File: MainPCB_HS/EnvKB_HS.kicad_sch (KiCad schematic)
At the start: 205 parts

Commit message: Added ANSI layout keys back.
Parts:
- added Stab5, Stab6: Stabilizer, Mounting_Keyboard_Stabilizer:Stabilizer_Cherry_MX_2u, symbol Mechanical:MountingHole
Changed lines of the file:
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@@
     (pin "2")
+  )
+  (symbol (lib_id "Mechanical:MountingHole") (at 172.72 259.842 0) (mirror x) (unit 1)
+    (in_bom yes) (on_board yes)
+    (property "Reference" "Stab5" (id 0) (at 170.2054 258.6736 0)
+      (effects (font (size 1.27 1.27)) (justify right))
+    )
+    (property "Value" "Stabilizer" (id 1) (at 170.2054 260.985 0)
+      (effects (font (size 1.27 1.27)) (justify right))
+    )
+    (property "Footprint" "Mounting_Keyboard_Stabilizer:Stabilizer_Cherry_MX_2u" (id 2) (at 172.72 259.842 0)
+      (effects (font (size 1.27 1.27)) hide)
+    )
+    (property "Datasheet" "~" (id 3) (at 172.72 259.842 0)
+      (effects (font (size 1.27 1.27)) hide)
+    )
   )
   (symbol (lib_id "Device:R_Small") (at 227.965 198.12 0) (unit 1)
@@
     (pin "1")
     (pin "2")
+  )
+  (symbol (lib_id "Mechanical:MountingHole") (at 187.198 259.842 0) (mirror x) (unit 1)
+    (in_bom yes) (on_board yes)
+    (property "Reference" "Stab6" (id 0) (at 184.6834 258.6736 0)
+      (effects (font (size 1.27 1.27)) (justify right))
+    )
+    (property "Value" "Stabilizer" (id 1) (at 184.6834 260.985 0)
+      (effects (font (size 1.27 1.27)) (justify right))
+    )
+    (property "Footprint" "Mounting_Keyboard_Stabilizer:Stabilizer_Cherry_MX_2u" (id 2) (at 187.198 259.842 0)
+      (effects (font (size 1.27 1.27)) hide)
+    )
+    (property "Datasheet" "~" (id 3) (at 187.198 259.842 0)
+      (effects (font (size 1.27 1.27)) hide)
+    )
   )
   (symbol (lib_id "Device:R_Small") (at 221.615 198.12 180) (unit 1)
@@
       (reference "Stab4") (unit 1) (value "Stabilizer") (footprint "Mounting_Keyboard_Stabilizer:Stabilizer_Cherry_MX_2u")
     )
+    (path "/49fb1b93-ef2c-4c13-8861-864d83ebc2ed"
+      (reference "Stab5") (unit 1) (value "Stabilizer") (footprint "Mounting_Keyboard_Stabilizer:Stabilizer_Cherry_MX_2u")
+    )
+    (path "/b0e410f9-6c63-4cdc-9525-c65e9116bb6a"
+      (reference "Stab6") (unit 1) (value "Stabilizer") (footprint "Mounting_Keyboard_Stabilizer:Stabilizer_Cherry_MX_2u")
+    )
     (path "/00000000-0000-0000-0000-000060ac4d40"

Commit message: fixed? ansi+iso+hotswap support I think but also file cleanup
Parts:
- D0, D1, D10, D11, D12, D13, D14, D15, D16, D17, D18, D19, D2, D20, D21, D22, D23, D24, D25, D26, D27, D28, D29, D3, D30, D31, D32, D33, D34, D35, D36, D37, D38, D39, D4, D40, D41, D42, D43, D44, D45, D46, D47, D48, D49, D5, D50, D51, D52, D53, D54, D55, D56, D57, D58, D59, D6, D60, D61, D62, D63, D64, D65, D66, D67, D68, D69, D7, D70, D71, D72, D73, D74, D75, D76, D77, D78, D79, D8, D80, D81, D82, D83, D84, D85, D86, D87, D88, D9: value D -> (none); footprint EM_Extras:SOD-123+D_DO-35_SOD27_P7.62mm_Horizontal -> (none)
- H0, H1, H10, H2, H3, H4, H5, H6, H7, H9: value MountingHole -> (none); footprint MountingHole:MountingHole_2.2mm_M2_Pad -> (none)
- K_0, K_1, K_10, K_11, K_12, K_13, K_14, K_15, K_16, K_17, K_18, K_19, K_2, K_20, K_21, K_22, K_23, K_24, K_25, K_26, K_27, K_28, K_29, K_3, K_30, K_31, K_32, K_33, K_34, K_35, K_36, K_37, K_38, K_39, K_4, K_40, K_41, K_42, K_43, K_44, K_45, K_46, K_47, K_48, K_49, K_5, K_50, K_51, K_52, K_53, K_54, K_55, K_56, K_57, K_58, K_59, K_6, K_60, K_61, K_62, K_64, K_64B1, K_65, K_66, K_67, K_68, K_69, K_7, K_70, K_71, K_72, K_73, K_74, K_75, K_76, K_77, K_78, K_79, K_8, K_80, K_81, K_82, K_83, K_84, K_85, K_86, K_87, K_88, K_9: value KEYSW -> (none); footprint MX_Only:MXOnly-1U-Hotswap-Modified -> (none); LCSC (none) -> C2803348
- K_63, K_63B1: value MX-NoLED -> (none); footprint MX_Only:MXOnly-1U-Hotswap-Modified -> (none); LCSC (none) -> C2803348
- LEDRESISTOR1: value 5.1K Resistor 1/4w -> (none); footprint Resistor_THT:R_Axial_DIN0207_L6.3mm_D2.5mm_P10.16mm_Horizontal -> (none)
- LEDRESISTOR2: value 5.1K Resistor 0805 -> (none); footprint Resistor_SMD:R_0805_2012Metric_Pad1.20x1.40mm_HandSolder -> (none)
- PowerLED0: value LED 3MM -> (none); footprint LED_THT:LED_D3.0mm_FlatTop -> (none)
- PowerLED1: value LED 0805 -> (none); footprint LED_SMD:LED_0805_2012Metric -> (none)
- RESISTOR0: value 5.1kohm 1/4w -> (none); footprint Resistor_THT:R_Axial_DIN0207_L6.3mm_D2.5mm_P10.16mm_Horizontal -> (none)
- RESISTOR1: value 5.1kohm 1/4 -> (none); footprint Resistor_THT:R_Axial_DIN0207_L6.3mm_D2.5mm_P10.16mm_Horizontal -> (none)
- RESISTOR2, RESISTOR3: value 5.1kohm 0805 -> (none); footprint Resistor_SMD:R_0805_2012Metric -> (none)
- RPI0: value Pico -> (none); footprint EM_Extras:RPi_Pico_SMD_TH -> (none)
- SW-RST0: value EVQ -> (none); footprint Button_Switch_SMD:Panasonic_EVQPUM_EVQPUD -> (none)
- Stab1: value Stabilizer -> (none); footprint Mounting_Keyboard_Stabilizer:Stabilizer_Cherry_MX_6.25u -> (none)
- Stab2, Stab3, Stab4, Stab5, Stab6: value Stabilizer -> (none); footprint Mounting_Keyboard_Stabilizer:Stabilizer_Cherry_MX_2u -> (none)
- USB1: value TYPE-C-31-M-14 -> (none); footprint josh-connectors:USB_C_TYPE-C-31-M-14 -> (none)

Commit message: roundified hotswap board and general corrections to other boards, RP2040 DRC fixes mainly
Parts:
- added D89: 1n4002, Diode_THT:D_DO-41_SOD81_P7.62mm_Horizontal, symbol Device:D_Small
- D0, D1, D10, D11, D12, D13, D14, D15, D16, D17, D18, D19, D2, D20, D21, D22, D23, D24, D25, D26, D27, D28, D29, D3, D30, D31, D32, D33, D34, D35, D36, D37, D38, D39, D4, D40, D41, D42, D43, D44, D45, D46, D47, D48, D49, D5, D50, D51, D52, D53, D54, D55, D56, D57, D58, D59, D6, D60, D61, D62, D63, D64, D65, D66, D67, D68, D69, D7, D70, D71, D72, D73, D74, D75, D76, D77, D78, D79, D8, D80, D81, D82, D83, D84, D85, D86, D87, D88, D9: value (none) -> D; footprint (none) -> EM_Extras:SOD-123+D_DO-35_SOD27_P7.62mm_Horizontal
- H0, H1, H10, H2, H3, H4, H5, H6, H7, H9: value (none) -> MountingHole; footprint (none) -> MountingHole:MountingHole_2.2mm_M2_Pad
- K_0, K_1, K_10, K_11, K_12, K_13, K_14, K_15, K_16, K_17, K_18, K_19, K_2, K_20, K_21, K_22, K_23, K_24, K_25, K_26, K_27, K_28, K_29, K_3, K_30, K_31, K_32, K_33, K_34, K_35, K_36, K_37, K_38, K_39, K_4, K_40, K_41, K_42, K_43, K_44, K_45, K_46, K_47, K_48, K_49, K_5, K_50, K_51, K_52, K_53, K_54, K_55, K_56, K_57, K_58, K_59, K_6, K_60, K_61, K_62, K_64, K_64B1, K_65, K_66, K_67, K_68, K_69, K_7, K_70, K_71, K_72, K_73, K_74, K_75, K_76, K_77, K_78, K_79, K_8, K_80, K_81, K_82, K_83, K_84, K_85, K_86, K_87, K_88, K_9: value (none) -> KEYSW; footprint (none) -> MX_Only:MXOnly-1U-Hotswap-Modified
- K_63, K_63B1: value (none) -> MX-NoLED; footprint (none) -> MX_Only:MXOnly-1U-Hotswap-Modified
- LEDRESISTOR1: value (none) -> 5.1K Resistor 1/4w; footprint (none) -> Resistor_THT:R_Axial_DIN0207_L6.3mm_D2.5mm_P10.16mm_Horizontal
- LEDRESISTOR2: value (none) -> 5.1K Resistor 0805; footprint (none) -> Resistor_SMD:R_0805_2012Metric_Pad1.20x1.40mm_HandSolder
- PowerLED0: value (none) -> LED 3MM; footprint (none) -> LED_THT:LED_D3.0mm_FlatTop
- PowerLED1: value (none) -> LED 0805; footprint (none) -> LED_SMD:LED_0805_2012Metric
- RESISTOR0: value (none) -> 5.1kohm 1/4w; footprint (none) -> Resistor_THT:R_Axial_DIN0207_L6.3mm_D2.5mm_P10.16mm_Horizontal
- RESISTOR1: value (none) -> 5.1kohm 1/4; footprint (none) -> Resistor_THT:R_Axial_DIN0207_L6.3mm_D2.5mm_P10.16mm_Horizontal
- RESISTOR2, RESISTOR3: value (none) -> 5.1kohm 0805; footprint (none) -> Resistor_SMD:R_0805_2012Metric
- RPI0: value (none) -> Pico; footprint (none) -> EM_Extras:RPi_Pico_SMD_TH
- SW-RST0: value (none) -> EVQ; footprint (none) -> Button_Switch_SMD:Panasonic_EVQPUM_EVQPUD
- Stab1: value (none) -> Stabilizer; footprint (none) -> Mounting_Keyboard_Stabilizer:Stabilizer_Cherry_MX_6.25u
- Stab2, Stab3, Stab4, Stab5, Stab6: value (none) -> Stabilizer; footprint (none) -> Mounting_Keyboard_Stabilizer:Stabilizer_Cherry_MX_2u
- USB1: value (none) -> TYPE-C-31-M-14; footprint (none) -> josh-connectors:USB_C_TYPE-C-31-M-14
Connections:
- net USBVBUS: now also D89.2 (A); no longer RPI0.40 (VBUS)
- net VSYS: now reaches RPI0.39 (VSYS)
- net VSYS: now also D89.1 (K)

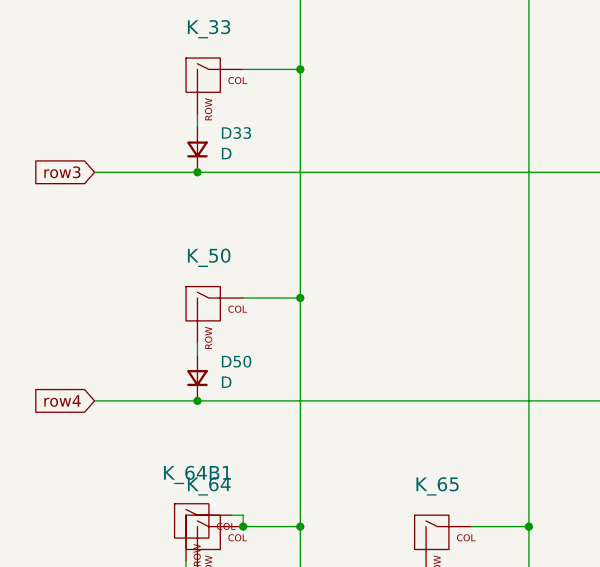
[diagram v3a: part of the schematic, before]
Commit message: Added Stepped left shift for orig version
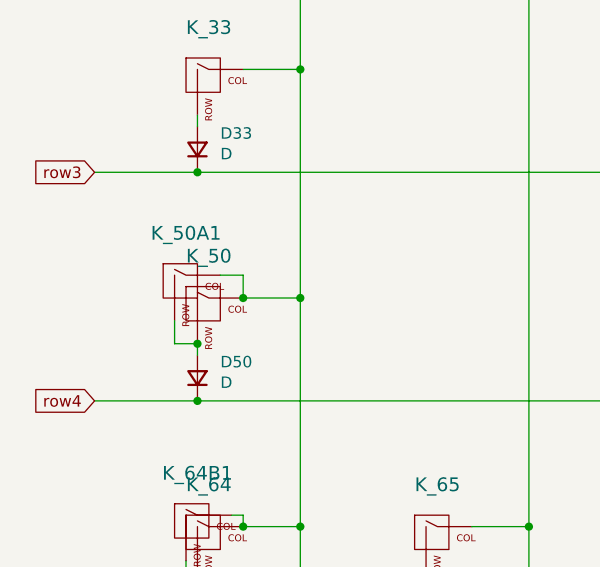
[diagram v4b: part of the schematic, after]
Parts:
- added K_50A1: KEYSW, MX_Only:MXOnly-1U-Hotswap-Modified, symbol MX_Alps_Hybrid:MX-NoLED
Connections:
- net col0: now also K_50A1.1 (COL)
- net at D50.2 (A), K_50.2 (ROW): now also K_50A1.2 (ROW)
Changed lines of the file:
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@@
   (junction (at 161.29 162.56) (diameter 0) (color 0 0 0 0)
   )
+  (junction (at 39.37 125.73) (diameter 0) (color 0 0 0 0)
+  )
   (junction (at 172.72 125.73) (diameter 0) (color 0 0 0 0)
   )
@@
   (junction (at 274.32 74.93) (diameter 0) (color 0 0 0 0)
   )
+  (junction (at 34.29 130.81) (diameter 0) (color 0 0 0 0)
+  )
   (junction (at 415.29 35.56) (diameter 0) (color 0 0 0 0)
   )
@@
     (stroke (width 0) (type default) (color 0 0 0 0))
   )
+  (wire (pts (xy 31.75 130.81) (xy 34.29 130.81))
+    (stroke (width 0) (type default) (color 0 0 0 0))
+  )
   (wire (pts (xy 110.49 137.16) (xy 135.89 137.16))
     (stroke (width 0) (type default) (color 0 0 0 0))
@@
     (stroke (width 0) (type default) (color 0 0 0 0))
   )
+  (wire (pts (xy 36.83 123.19) (xy 39.37 123.19))
+    (stroke (width 0) (type default) (color 0 0 0 0))
+  )
+  (wire (pts (xy 39.37 123.19) (xy 39.37 125.73))
+    (stroke (width 0) (type default) (color 0 0 0 0))
+  )
   (wire (pts (xy 221.615 200.66) (xy 221.615 201.295))
     (stroke (width 0) (type default) (color 0 0 0 0))
@@
     (stroke (width 0) (type default) (color 0 0 0 0))
   )
+  (wire (pts (xy 31.75 128.27) (xy 31.75 130.81))
+    (stroke (width 0) (type default) (color 0 0 0 0))
+  )
   (wire (pts (xy 191.77 125.73) (xy 198.12 125.73))
     (stroke (width 0) (type default) (color 0 0 0 0))
@@
     (pin "2")
   )
+  (symbol (lib_id "MX_Alps_Hybrid:MX-NoLED") (at 33.02 124.46 0) (unit 1)
+    (in_bom yes) (on_board yes)
+    (property "Reference" "K_50A1" (id 0) (at 33.02 118.5418 0)
+      (effects (font (size 1.524 1.524)))
+    )
+    (property "Value" "KEYSW" (id 1) (at 33.02 127 0)
+      (effects (font (size 1.524 1.524)) hide)
+    )
+    (property "Footprint" "MX_Only:MXOnly-1U-Hotswap-Modified" (id 2) (at 33.02 124.46 0)
+      (effects (font (size 1.524 1.524)) hide)
+    )
+    (property "Datasheet" "" (id 3) (at 33.02 124.46 0)
+      (effects (font (size 1.524 1.524)))
+    )
+    (property "LCSC" "C2803348" (id 4) (at 33.02 124.46 0)
+      (effects (font (size 1.27 1.27)) hide)
+    )
+    (pin "1")
+    (pin "2")
+  )
   (symbol (lib_id "Mechanical:MountingHole") (at 172.72 259.842 0) (mirror x) (unit 1)
     (in_bom yes) (on_board yes)
@@
       (reference "K_50") (unit 1) (value "KEYSW") (footprint "MX_Only:MXOnly-1U-Hotswap-Modified")
     )
+    (path "/413bf164-96e1-4397-9fa3-f110780c247f"
+      (reference "K_50A1") (unit 1) (value "KEYSW") (footprint "MX_Only:MXOnly-1U-Hotswap-Modified")
+    )
     (path "/00000000-0000-0000-0000-000000000511"

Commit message: enlarged mount holes on HS version + increased clearance on some traces between diodes and plates holes, need to do this for whole board though
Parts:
- H0, H1, H10, H2, H3, H4, H5, H6, H7, H9: footprint MountingHole:MountingHole_2.2mm_M2_Pad -> MountingHole:MountingHole_3.7mm_Pad
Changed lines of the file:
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@@
       (effects (font (size 1.27 1.27)) (justify left))
     )
-    (property "Footprint" "MountingHole:MountingHole_2.2mm_M2_Pad" (id 2) (at 147.32 270.51 0)
+    (property "Footprint" "MountingHole:MountingHole_3.7mm_Pad" (id 2) (at 147.32 270.51 0)
       (effects (font (size 1.27 1.27)) hide)
     )
@@
       (effects (font (size 1.27 1.27)) (justify left))
     )
-    (property "Footprint" "MountingHole:MountingHole_2.2mm_M2_Pad" (id 2) (at 137.16 270.51 0)
+    (property "Footprint" "MountingHole:MountingHole_3.7mm_Pad" (id 2) (at 137.16 270.51 0)
       (effects (font (size 1.27 1.27)) hide)
     )
@@
       (effects (font (size 1.27 1.27)) (justify left))
     )
-    (property "Footprint" "MountingHole:MountingHole_2.2mm_M2_Pad" (id 2) (at 142.24 270.51 0)
+    (property "Footprint" "MountingHole:MountingHole_3.7mm_Pad" (id 2) (at 142.24 270.51 0)
       (effects (font (size 1.27 1.27)) hide)
     )
@@
       (effects (font (size 1.27 1.27)) (justify left))
     )
-    (property "Footprint" "MountingHole:MountingHole_2.2mm_M2_Pad" (id 2) (at 152.4 270.51 0)
+    (property "Footprint" "MountingHole:MountingHole_3.7mm_Pad" (id 2) (at 152.4 270.51 0)
       (effects (font (size 1.27 1.27)) hide)
     )
@@
       (effects (font (size 1.27 1.27)) (justify left))
     )
-    (property "Footprint" "MountingHole:MountingHole_2.2mm_M2_Pad" (id 2) (at 167.64 270.51 0)
+    (property "Footprint" "MountingHole:MountingHole_3.7mm_Pad" (id 2) (at 167.64 270.51 0)
       (effects (font (size 1.27 1.27)) hide)
     )
@@
       (effects (font (size 1.27 1.27)) (justify left))
     )
-    (property "Footprint" "MountingHole:MountingHole_2.2mm_M2_Pad" (id 2) (at 172.72 270.51 0)
+    (property "Footprint" "MountingHole:MountingHole_3.7mm_Pad" (id 2) (at 172.72 270.51 0)
       (effects (font (size 1.27 1.27)) hide)
     )
@@
       (effects (font (size 1.27 1.27)) (justify left))
     )
-    (property "Footprint" "MountingHole:MountingHole_2.2mm_M2_Pad" (id 2) (at 157.48 270.51 0)
+    (property "Footprint" "MountingHole:MountingHole_3.7mm_Pad" (id 2) (at 157.48 270.51 0)
       (effects (font (size 1.27 1.27)) hide)
     )
@@
       (effects (font (size 1.27 1.27)) (justify left))
     )
-    (property "Footprint" "MountingHole:MountingHole_2.2mm_M2_Pad" (id 2) (at 162.56 270.51 0)
+    (property "Footprint" "MountingHole:MountingHole_3.7mm_Pad" (id 2) (at 162.56 270.51 0)
       (effects (font (size 1.27 1.27)) hide)
     )
@@
       (effects (font (size 1.27 1.27)) (justify left))
     )
-    (property "Footprint" "MountingHole:MountingHole_2.2mm_M2_Pad" (id 2) (at 132.08 270.51 0)
+    (property "Footprint" "MountingHole:MountingHole_3.7mm_Pad" (id 2) (at 132.08 270.51 0)
       (effects (font (size 1.27 1.27)) hide)
     )
@@
       (effects (font (size 1.27 1.27)) (justify left))
     )
-    (property "Footprint" "MountingHole:MountingHole_2.2mm_M2_Pad" (id 2) (at 127 270.51 0)
+    (property "Footprint" "MountingHole:MountingHole_3.7mm_Pad" (id 2) (at 127 270.51 0)
       (effects (font (size 1.27 1.27)) hide)
     )
@@
     )
     (path "/00000000-0000-0000-0000-0000605938c3"
-      (reference "H0") (unit 1) (value "MountingHole") (footprint "MountingHole:MountingHole_2.2mm_M2_Pad")
+      (reference "H0") (unit 1) (value "MountingHole") (footprint "MountingHole:MountingHole_3.7mm_Pad")
     )
     (path "/00000000-0000-0000-0000-0000605bd366"
-      (reference "H1") (unit 1) (value "MountingHole") (footprint "MountingHole:MountingHole_2.2mm_M2_Pad")
+      (reference "H1") (unit 1) (value "MountingHole") (footprint "MountingHole:MountingHole_3.7mm_Pad")
     )
     (path "/00000000-0000-0000-0000-000061411d60"
-      (reference "H2") (unit 1) (value "MountingHole") (footprint "MountingHole:MountingHole_2.2mm_M2_Pad")
+      (reference "H2") (unit 1) (value "MountingHole") (footprint "MountingHole:MountingHole_3.7mm_Pad")
     )
     (path "/00000000-0000-0000-0000-00006058bc08"
-      (reference "H3") (unit 1) (value "MountingHole") (footprint "MountingHole:MountingHole_2.2mm_M2_Pad")
+      (reference "H3") (unit 1) (value "MountingHole") (footprint "MountingHole:MountingHole_3.7mm_Pad")
     )
     (path "/00000000-0000-0000-0000-00006068a680"
-      (reference "H4") (unit 1) (value "MountingHole") (footprint "MountingHole:MountingHole_2.2mm_M2_Pad")
+      (reference "H4") (unit 1) (value "MountingHole") (footprint "MountingHole:MountingHole_3.7mm_Pad")
     )
     (path "/00000000-0000-0000-0000-00006162a1bf"
-      (reference "H5") (unit 1) (value "MountingHole") (footprint "MountingHole:MountingHole_2.2mm_M2_Pad")
+      (reference "H5") (unit 1) (value "MountingHole") (footprint "MountingHole:MountingHole_3.7mm_Pad")
     )
     (path "/00000000-0000-0000-0000-000060748b43"
-      (reference "H6") (unit 1) (value "MountingHole") (footprint "MountingHole:MountingHole_2.2mm_M2_Pad")
+      (reference "H6") (unit 1) (value "MountingHole") (footprint "MountingHole:MountingHole_3.7mm_Pad")
     )
     (path "/00000000-0000-0000-0000-00006077360a"
-      (reference "H7") (unit 1) (value "MountingHole") (footprint "MountingHole:MountingHole_2.2mm_M2_Pad")
+      (reference "H7") (unit 1) (value "MountingHole") (footprint "MountingHole:MountingHole_3.7mm_Pad")
     )
     (path "/00000000-0000-0000-0000-000060717f95"
-      (reference "H9") (unit 1) (value "MountingHole") (footprint "MountingHole:MountingHole_2.2mm_M2_Pad")
+      (reference "H9") (unit 1) (value "MountingHole") (footprint "MountingHole:MountingHole_3.7mm_Pad")
     )
     (path "/00000000-0000-0000-0000-0000607429b3"
-      (reference "H10") (unit 1) (value "MountingHole") (footprint "MountingHole:MountingHole_2.2mm_M2_Pad")
+      (reference "H10") (unit 1) (value "MountingHole") (footprint "MountingHole:MountingHole_3.7mm_Pad")
     )
     (path "/00000000-0000-0000-0000-0000603522c8"

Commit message: huge repo cleanup
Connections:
- net LEDPIN: no longer names the net of RPI0.1 (GPIO0)
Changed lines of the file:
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@@
-    (stroke (width 0) (type default) (color 0 0 0 0))
-  )
-  (wire (pts (xy 22.86 60.96) (xy 60.96 60.96))
     (stroke (width 0) (type default) (color 0 0 0 0))
   )
@@
     (effects (font (size 1.27 1.27)) (justify right))
     (property "Intersheet References" "${INTERSHEET_REFS}" (id 0) (at 0 0 0)
-      (effects (font (size 1.27 1.27)) hide)
-    )
-  )
-  (global_label "LEDPIN" (shape input) (at 311.15 231.14 180) (fields_autoplaced)
-    (effects (font (size 1.27 1.27)) (justify right))
-    (property "Intersheet References" "${INTERSHEET_REFS}" (id 0) (at 0 0 0)
-      (effects (font (size 1.27 1.27)) hide)
-    )
-  )
-  (global_label "row1" (shape input) (at 22.86 60.96 180) (fields_autoplaced)
-    (effects (font (size 1.27 1.27)) (justify right))
-    (property "Intersheet References" "${INTERSHEET_REFS}" (id 0) (at 0 0 0)

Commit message: lots more work towards making this available
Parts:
- LEDRESISTOR1: value 5.1K Resistor 1/4w -> 5.1kohm 1/4w; footprint Resistor_THT:R_Axial_DIN0207_L6.3mm_D2.5mm_P10.16mm_Horizontal -> Resistor_THT:R_Axial_DIN0207_L6.3mm_D2.5mm_P7.62mm_Horizontal
- RESISTOR0: footprint Resistor_THT:R_Axial_DIN0207_L6.3mm_D2.5mm_P10.16mm_Horizontal -> Resistor_THT:R_Axial_DIN0207_L6.3mm_D2.5mm_P7.62mm_Horizontal
- RESISTOR1: value 5.1kohm 1/4 -> 5.1kohm 1/4w; footprint Resistor_THT:R_Axial_DIN0207_L6.3mm_D2.5mm_P10.16mm_Horizontal -> Resistor_THT:R_Axial_DIN0207_L6.3mm_D2.5mm_P7.62mm_Horizontal
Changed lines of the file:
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@@
     (in_bom yes) (on_board yes)
     (property "Reference" "LEDRESISTOR1" (id 0) (at 223.52 255.27 90))
-    (property "Value" "5.1K Resistor 1/4w" (id 1) (at 218.44 256.54 90)
-      (effects (font (size 1.27 1.27)) hide)
-    )
-    (property "Footprint" "Resistor_THT:R_Axial_DIN0207_L6.3mm_D2.5mm_P10.16mm_Horizontal" (id 2) (at 217.17 252.73 0)
+    (property "Value" "5.1kohm 1/4w" (id 1) (at 218.44 256.54 90)
+      (effects (font (size 1.27 1.27)) hide)
+    )
+    (property "Footprint" "Resistor_THT:R_Axial_DIN0207_L6.3mm_D2.5mm_P7.62mm_Horizontal" (id 2) (at 217.17 252.73 0)
       (effects (font (size 1.27 1.27)) hide)
     )
@@
       (effects (font (size 0.9906 0.9906)) hide)
     )
-    (property "Value" "5.1kohm 1/4" (id 1) (at 226.06 195.58 90)
+    (property "Value" "5.1kohm 1/4w" (id 1) (at 226.06 195.58 90)
       (effects (font (size 0.762 0.762)) hide)
     )
-    (property "Footprint" "Resistor_THT:R_Axial_DIN0207_L6.3mm_D2.5mm_P10.16mm_Horizontal" (id 2) (at 226.06 198.12 0)
+    (property "Footprint" "Resistor_THT:R_Axial_DIN0207_L6.3mm_D2.5mm_P7.62mm_Horizontal" (id 2) (at 226.06 198.12 0)
       (effects (font (size 1.27 1.27)) hide)
     )
@@
       (effects (font (size 1.27 1.27)) hide)
     )
-    (property "Footprint" "Resistor_THT:R_Axial_DIN0207_L6.3mm_D2.5mm_P10.16mm_Horizontal" (id 2) (at 223.52 198.12 0)
+    (property "Footprint" "Resistor_THT:R_Axial_DIN0207_L6.3mm_D2.5mm_P7.62mm_Horizontal" (id 2) (at 223.52 198.12 0)
       (effects (font (size 1.27 1.27)) hide)
     )
@@
     )
     (path "/00000000-0000-0000-0000-0000604a80b1"
-      (reference "LEDRESISTOR1") (unit 1) (value "5.1K Resistor 1/4w") (footprint "Resistor_THT:R_Axial_DIN0207_L6.3mm_D2.5mm_P10.16mm_Horizontal")
+      (reference "LEDRESISTOR1") (unit 1) (value "5.1kohm 1/4w") (footprint "Resistor_THT:R_Axial_DIN0207_L6.3mm_D2.5mm_P7.62mm_Horizontal")
     )
     (path "/1cc562ed-98f7-4977-9171-841bb0ee9efc"
@@
     )
     (path "/00000000-0000-0000-0000-00006066af89"
-      (reference "RESISTOR0") (unit 1) (value "5.1kohm 1/4w") (footprint "Resistor_THT:R_Axial_DIN0207_L6.3mm_D2.5mm_P10.16mm_Horizontal")
+      (reference "RESISTOR0") (unit 1) (value "5.1kohm 1/4w") (footprint "Resistor_THT:R_Axial_DIN0207_L6.3mm_D2.5mm_P7.62mm_Horizontal")
     )
     (path "/00000000-0000-0000-0000-0000606333e5"
-      (reference "RESISTOR1") (unit 1) (value "5.1kohm 1/4") (footprint "Resistor_THT:R_Axial_DIN0207_L6.3mm_D2.5mm_P10.16mm_Horizontal")
+      (reference "RESISTOR1") (unit 1) (value "5.1kohm 1/4w") (footprint "Resistor_THT:R_Axial_DIN0207_L6.3mm_D2.5mm_P7.62mm_Horizontal")
     )
     (path "/d3060307-2c26-4d91-931e-3ca65ef351b7"
